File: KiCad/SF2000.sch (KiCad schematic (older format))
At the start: 45 parts, among them J1 Conn_2Rows-86Pins_even_odd, J2 Conn_01x02, U1 LM1117-3.3, U2 TPS73643DBV, U3 SN74CBT16211, U4 SN74CBT16211, U5 SN74CBT16211, U6 SN74AUP1T87DCKR

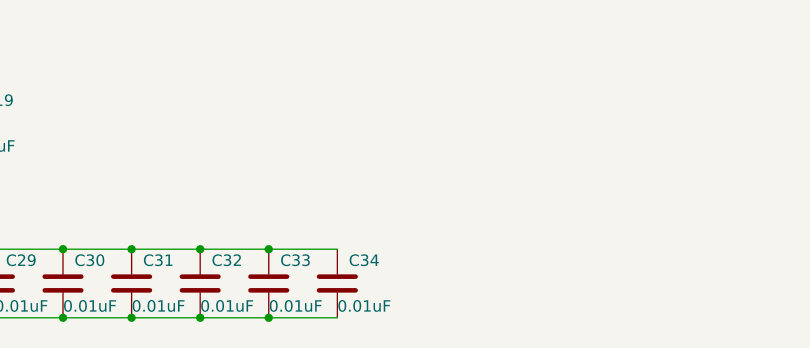
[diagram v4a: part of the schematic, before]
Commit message: added JTAG-header, jumpers and pull-up-resistors
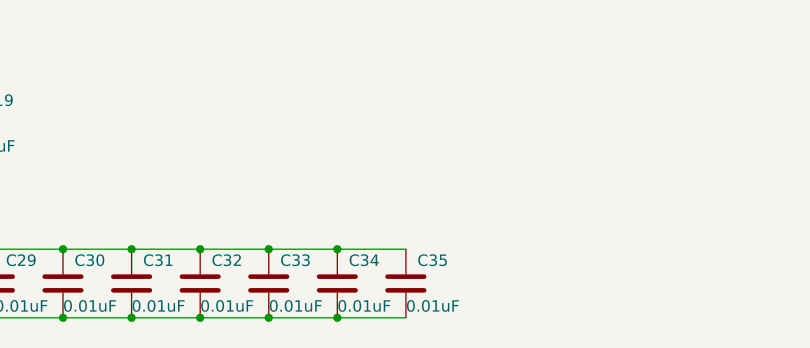
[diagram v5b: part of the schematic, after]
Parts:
- added C35: 0.01uF, Capacitor_SMD:C_0805_2012Metric_Pad1.15x1.40mm_HandSolder, symbol Device:C
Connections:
- net 3V3: now also C35.2
- net GND: now also C35.1
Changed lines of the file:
@@
 Wire Wire Line
 	5100 7450 4800 7450
+$Comp
+L Device:C C35
+U 1 1 6263A5BF
+P 5700 7300
+F 0 "C35" H 5750 7400 50  0000 L CNN
+F 1 "0.01uF" H 5700 7200 50  0000 L CNN
+F 2 "Capacitor_SMD:C_0805_2012Metric_Pad1.15x1.40mm_HandSolder" H 5738 7150 50  0001 C CNN
+F 3 "~" H 5700 7300 50  0001 C CNN
+	1    5700 7300
+	1    0    0    -1
+$EndComp
+Wire Wire Line
+	5400 7150 5700 7150
+Connection ~ 5400 7150
+Wire Wire Line
+	5400 7450 5700 7450
+Connection ~ 5400 7450
 $EndSCHEMATC

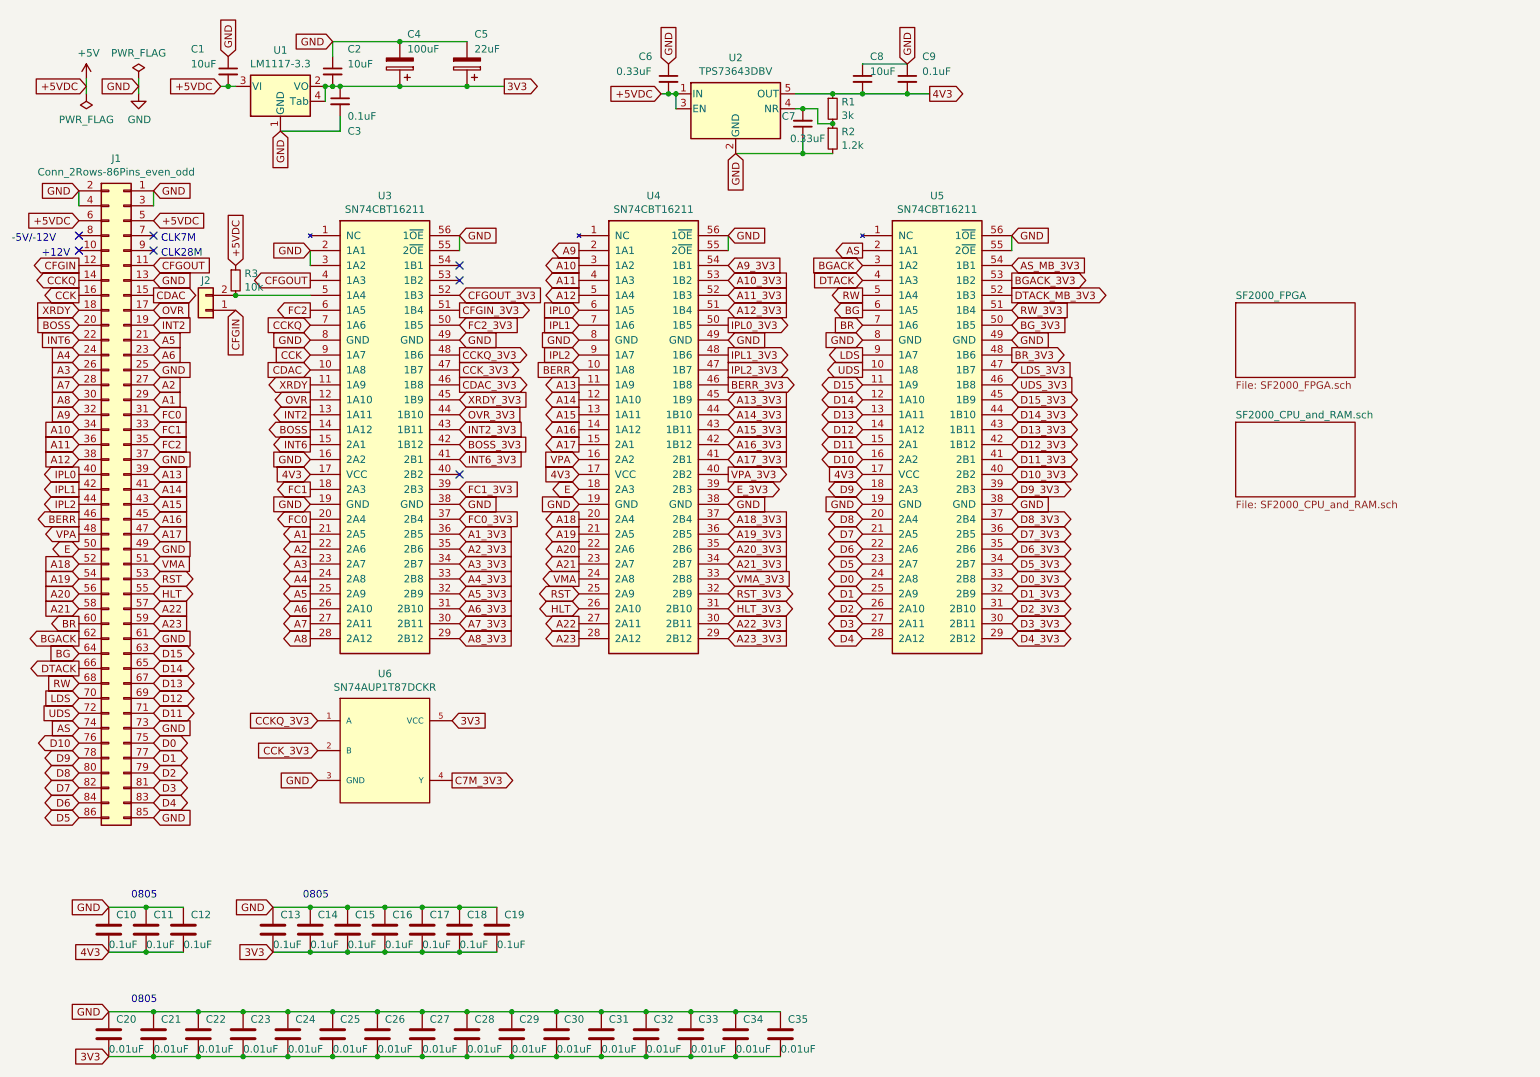
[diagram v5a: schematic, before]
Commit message: added buffering for IDE, rearranged components a bit and did more routing
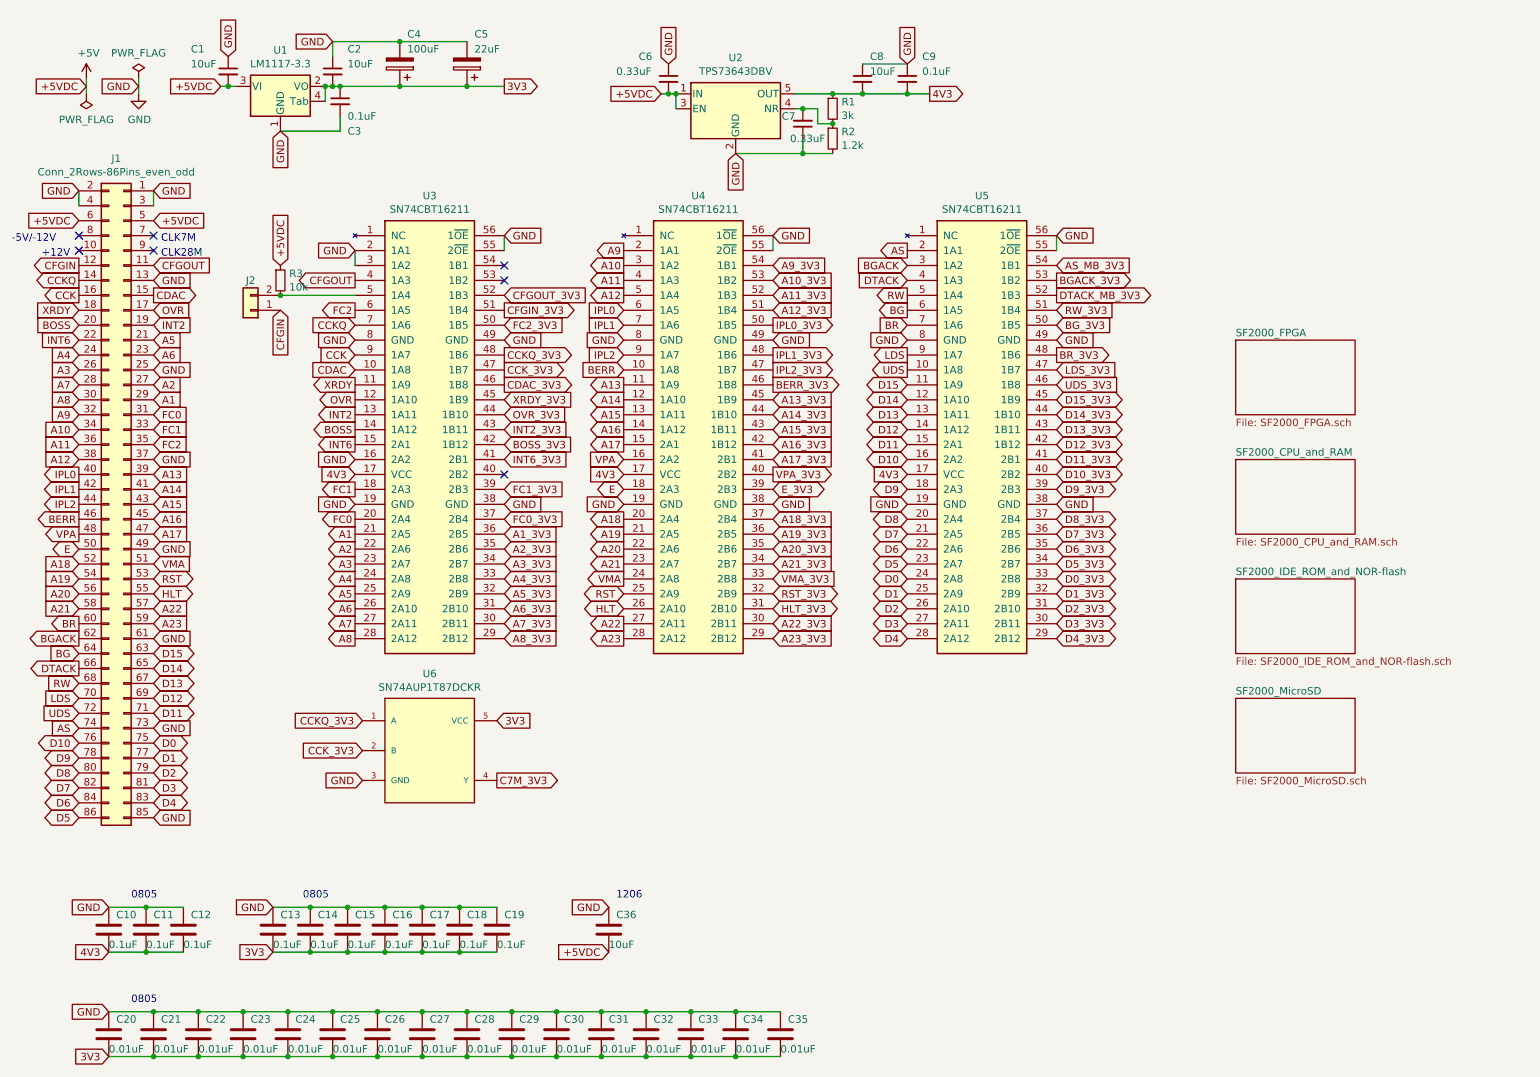
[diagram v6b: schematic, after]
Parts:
- added C36: 10uF, Capacitor_SMD:C_1206_3216Metric_Pad1.42x1.75mm_HandSolder, symbol Device:C
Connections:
- net +5V: now also C36.2
- net GND: now also C36.1
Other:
- note added: "1206"
- moved on the sheet: J2, R3, U3, U4, U5, U6

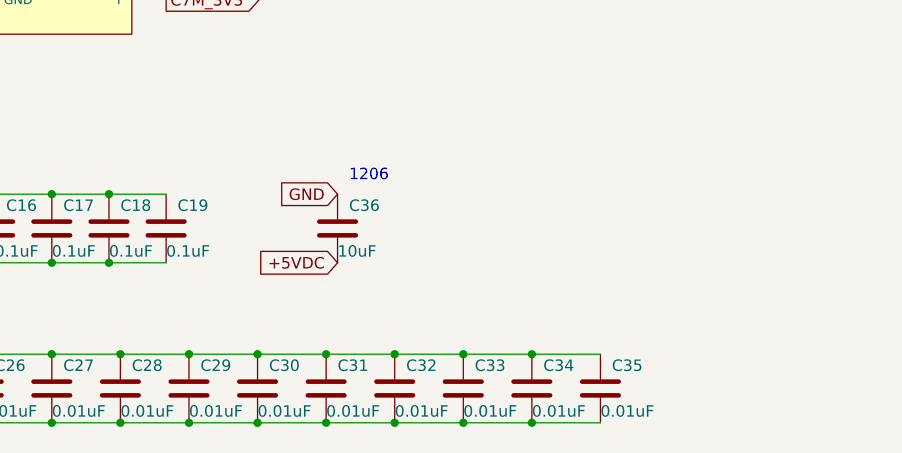
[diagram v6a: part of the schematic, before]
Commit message: more routing and added two capacitors
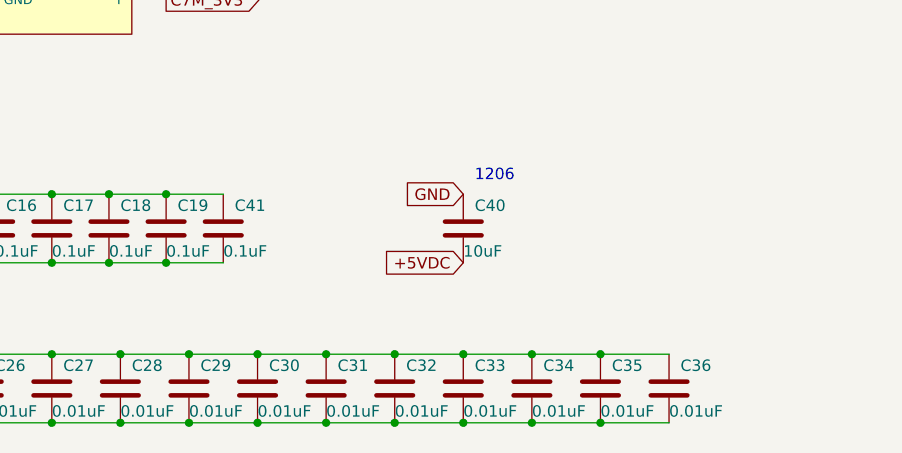
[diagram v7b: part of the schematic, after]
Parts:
- added C36: 0.01uF, Capacitor_SMD:C_0805_2012Metric_Pad1.15x1.40mm_HandSolder, symbol Device:C
- added C41: 0.1uF, Capacitor_SMD:C_0805_2012Metric_Pad1.15x1.40mm_HandSolder, symbol Device:C
- renumbered C36 to C40
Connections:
- net 3V3: now also C36.2, C41.2
- net GND: now also C36.1, C41.1
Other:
- moved on the sheet: C40
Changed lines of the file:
@@
 $EndSheet
 $Comp
-L Device:C C36
+L Device:C C40
 U 1 1 628C0969
-P 4550 6600
-F 0 "C36" H 4600 6700 50  0000 L CNN
-F 1 "10uF" H 4550 6500 50  0000 L CNN
-F 2 "Capacitor_SMD:C_1206_3216Metric_Pad1.42x1.75mm_HandSolder" H 4588 6450 50  0001 C CNN
-F 3 "~" H 4550 6600 50  0001 C CNN
-	1    4550 6600
+P 5100 6600
+F 0 "C40" H 5150 6700 50  0000 L CNN
+F 1 "10uF" H 5100 6500 50  0000 L CNN
+F 2 "Capacitor_SMD:C_1206_3216Metric_Pad1.42x1.75mm_HandSolder" H 5138 6450 50  0001 C CNN
+F 3 "~" H 5100 6600 50  0001 C CNN
+	1    5100 6600
 	1    0    0    -1
 $EndComp
-Text GLabel 4550 6450 0    50   Input ~ 0
+Text GLabel 5100 6450 0    50   Input ~ 0
 GND
-Text GLabel 4550 6750 0    50   Input ~ 0
+Text GLabel 5100 6750 0    50   Input ~ 0
 +5VDC
-Text Notes 4600 6400 0    50   ~ 0
+Text Notes 5150 6400 0    50   ~ 0
 1206
+$Comp
+L Device:C C41
+U 1 1 620E9DC4
+P 4050 6600
+F 0 "C41" H 4100 6700 50  0000 L CNN
+F 1 "0.1uF" H 4050 6500 50  0000 L CNN
+F 2 "Capacitor_SMD:C_0805_2012Metric_Pad1.15x1.40mm_HandSolder" H 4088 6450 50  0001 C CNN
+F 3 "~" H 4050 6600 50  0001 C CNN
+	1    4050 6600
+	1    0    0    -1
+$EndComp
+Wire Wire Line
+	3800 6450 4050 6450
+Connection ~ 3800 6450
+Wire Wire Line
+	3800 6750 4050 6750
+Connection ~ 3800 6750
+$Comp
+L Device:C C36
+U 1 1 62106B38
+P 6000 7300
+F 0 "C36" H 6050 7400 50  0000 L CNN
+F 1 "0.01uF" H 6000 7200 50  0000 L CNN
+F 2 "Capacitor_SMD:C_0805_2012Metric_Pad1.15x1.40mm_HandSolder" H 6038 7150 50  0001 C CNN
+F 3 "~" H 6000 7300 50  0001 C CNN
+	1    6000 7300
+	1    0    0    -1
+$EndComp
+Wire Wire Line
+	5700 7150 6000 7150
+Connection ~ 5700 7150
+Wire Wire Line
+	5700 7450 6000 7450
+Connection ~ 5700 7450
 $EndSCHEMATC

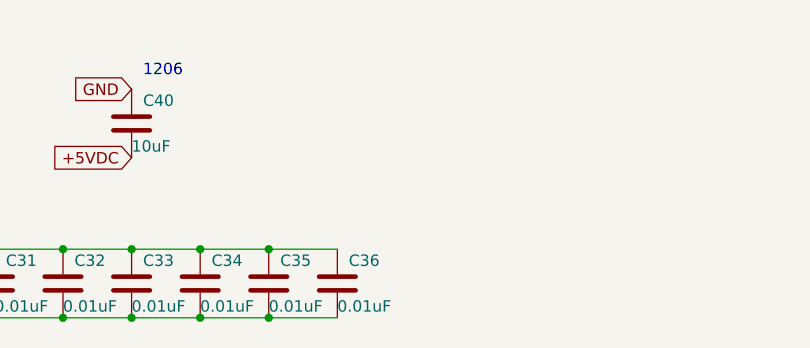
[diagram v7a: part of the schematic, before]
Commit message: added capacitor for FPGA VCC-pin 128
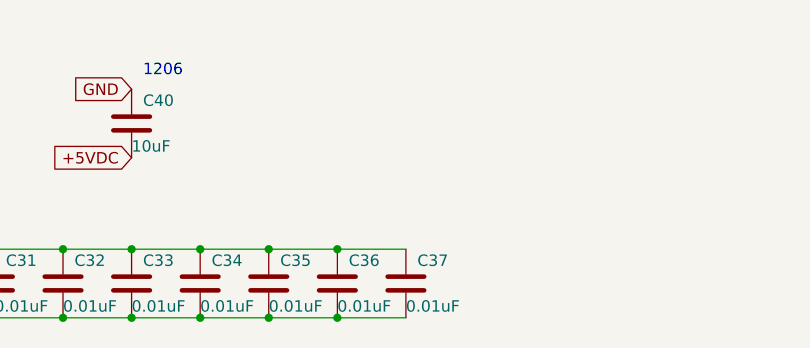
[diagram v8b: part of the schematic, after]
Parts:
- added C37: 0.01uF, Capacitor_SMD:C_0805_2012Metric_Pad1.15x1.40mm_HandSolder, symbol Device:C
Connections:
- net 3V3: now also C37.2
- net GND: now also C37.1
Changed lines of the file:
@@
 	5700 7450 6000 7450
 Connection ~ 5700 7450
+$Comp
+L Device:C C37
+U 1 1 621C2B09
+P 6300 7300
+F 0 "C37" H 6350 7400 50  0000 L CNN
+F 1 "0.01uF" H 6300 7200 50  0000 L CNN
+F 2 "Capacitor_SMD:C_0805_2012Metric_Pad1.15x1.40mm_HandSolder" H 6338 7150 50  0001 C CNN
+F 3 "~" H 6300 7300 50  0001 C CNN
+	1    6300 7300
+	1    0    0    -1
+$EndComp
+Wire Wire Line
+	6000 7150 6300 7150
+Connection ~ 6000 7150
+Wire Wire Line
+	6000 7450 6300 7450
+Connection ~ 6000 7450
 $EndSCHEMATC
